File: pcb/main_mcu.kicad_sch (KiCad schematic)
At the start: 16 parts, among them U3 STM32H563VITx

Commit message: tons of work on rf and mcu
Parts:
- added C37, C38: 8pF, symbol Device:C_Small
- added C39, C40: 17pF, symbol Device:C_Small
- added R12, R13: 1k, symbol Device:R_Small
- added Y1: 25mHz 8pf, symbol Device:Crystal_GND24
- added Y2: 32.768kHz 12.5pF, symbol Device:Crystal
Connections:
- net GND: now also C37.2, C38.1, C39.2, C40.1, Y1.2 (G), Y1.4 (G)
- net hse_0: now reaches U3.12 (PH0)
- net hse_0: now also C38.2, Y1.1
- net at U3.13 (PH1): now also R12.2
- net usb1_d-: now reaches U3.70 (PA11)
- net usb1_d+: now reaches U3.71 (PA12)
- net lse_0: now reaches U3.8 (PC14)
- net lse_0: now also C40.2, Y2.1
- net at U3.9 (PC15): now also R13.1
- new net hse_1: C37.1, R12.1, Y1.3
- new net lse_1: C39.1, R13.2, Y2.2
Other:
- note added: "todo: figure out if series resistors are necessary"
- moved on the sheet: C12, C13, U3

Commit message: added missing files, rf stuff done I think (hope)
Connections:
- net gps_tx: now reaches U3.55 (PD8)
- net gps_rx: now reaches U3.56 (PD9)
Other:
- note added: "hse"
- note added: "lse"
- moved on the sheet: C37, C38, Y1

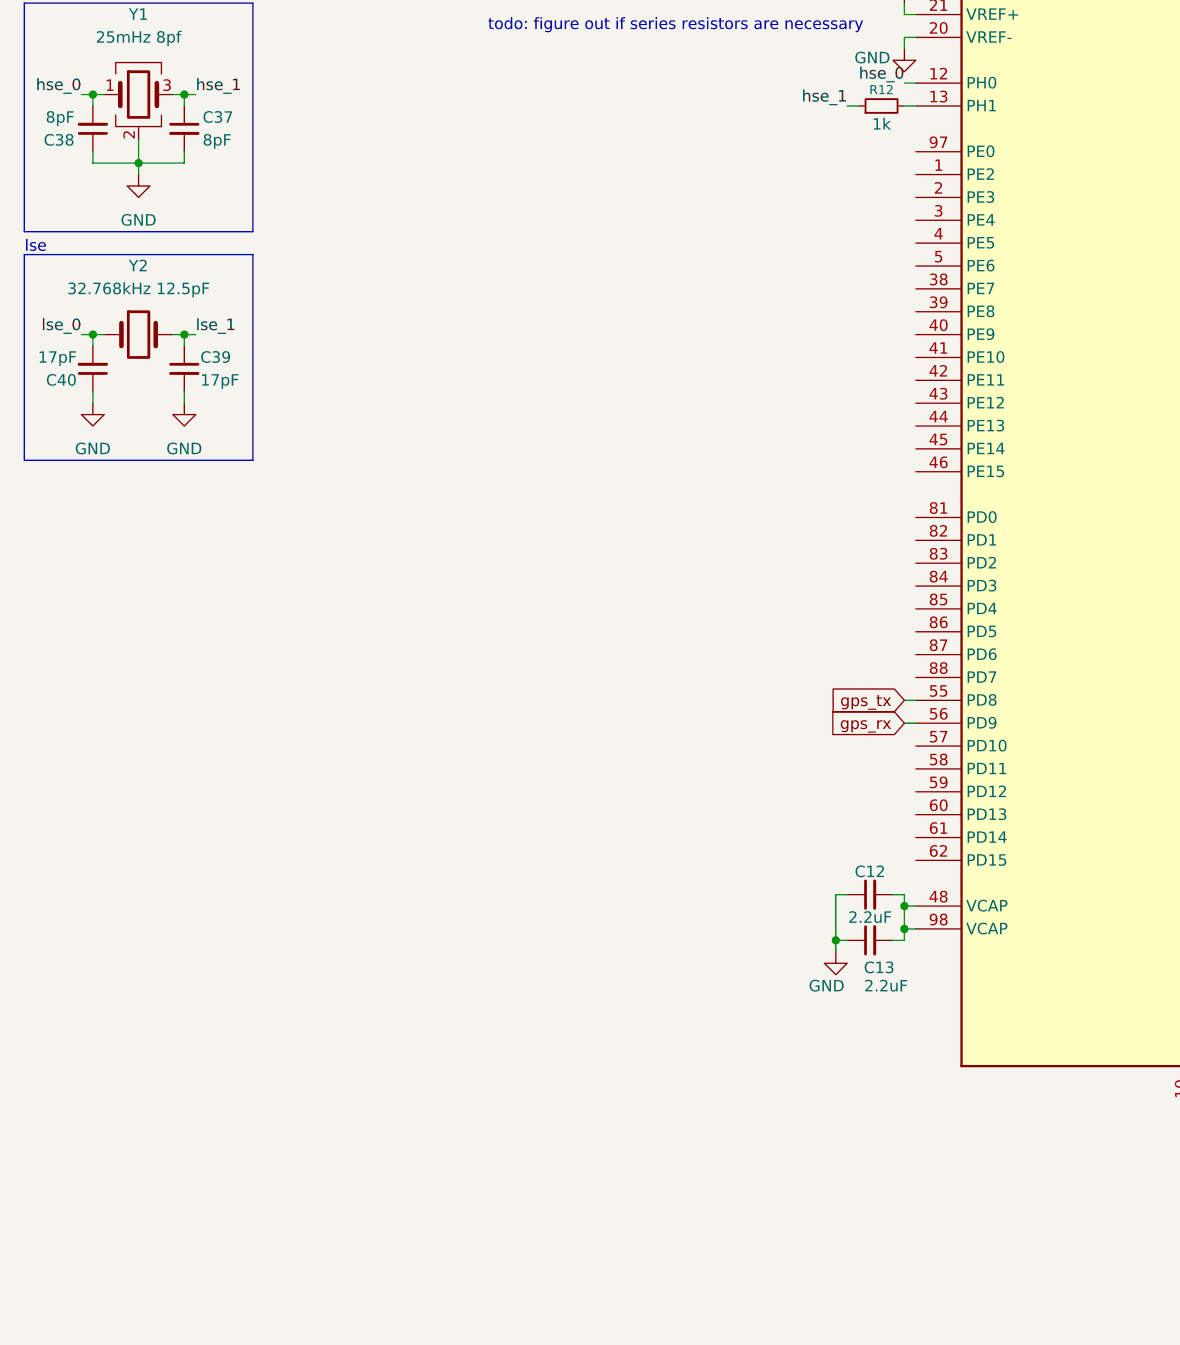
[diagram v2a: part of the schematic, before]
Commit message: sensors pretty much done (still need to add high g_
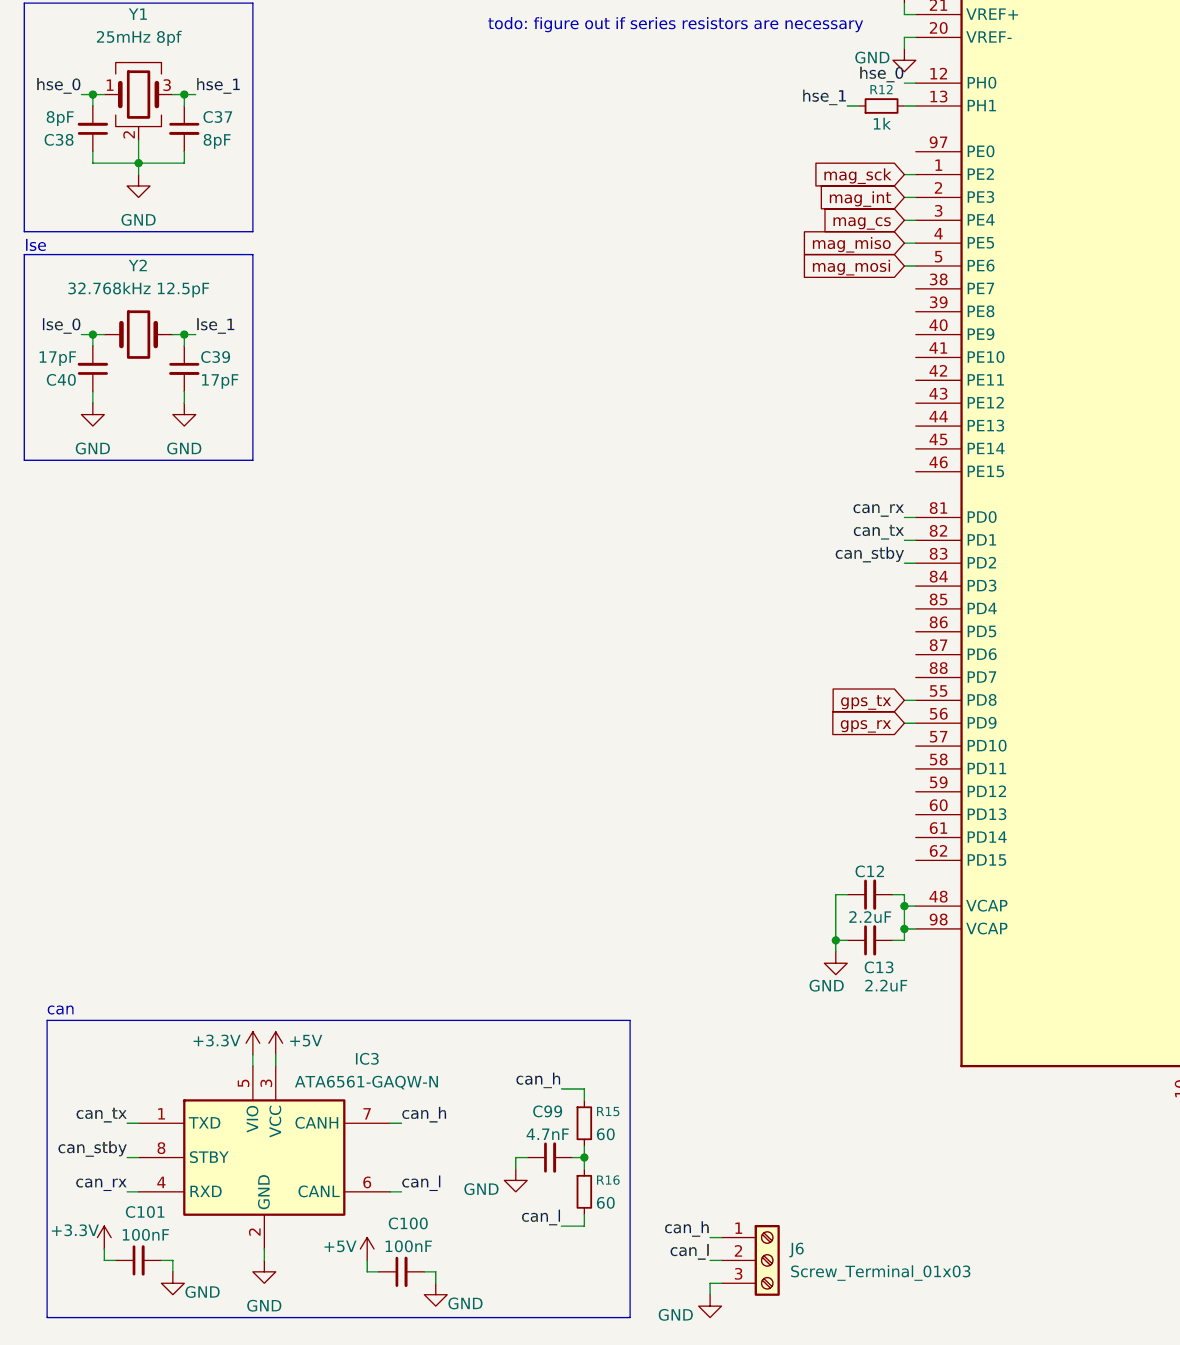
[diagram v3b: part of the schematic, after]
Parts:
- added C100, C101: 100nF, symbol Device:C_Small
- added C99: 4.7nF, symbol Device:C_Small
- added IC3: ATA6561-GAQW-N, SOIC127P600X175-8N, symbol ATA6561-GAQW-N:ATA6561-GAQW-N
- added J6: Screw_Terminal_01x03, symbol Connector:Screw_Terminal_01x03
- added R15, R16: 60, symbol Device:R_Small
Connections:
- net +3.3V: now also C101.1, IC3.5 (VIO)
- net GND: now also C100.2, C101.2, C99.1, IC3.2 (GND), J6.3 (Pin_3)
- net mag_sck: now reaches U3.1 (PE2)
- net mag_int: now reaches U3.2 (PE3)
- net mag_cs: now reaches U3.3 (PE4)
- net mag_miso: now reaches U3.4 (PE5)
- net mag_mosi: now reaches U3.5 (PE6)
- net can_rx: now reaches U3.81 (PD0)
- net can_rx: now also IC3.4 (RXD)
- net can_tx: now reaches U3.82 (PD1)
- net can_tx: now also IC3.1 (TXD)
- net can_stby: now reaches U3.83 (PD2)
- net can_stby: now also IC3.8 (STBY)
- new net: C99.2, R15.2, R16.1
- new net +5V: C100.1, IC3.3 (VCC)
- new net can_h: IC3.7 (CANH), J6.1 (Pin_1), R15.1
- new net can_l: IC3.6 (CANL), J6.2 (Pin_2), R16.2
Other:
- note added: "can"

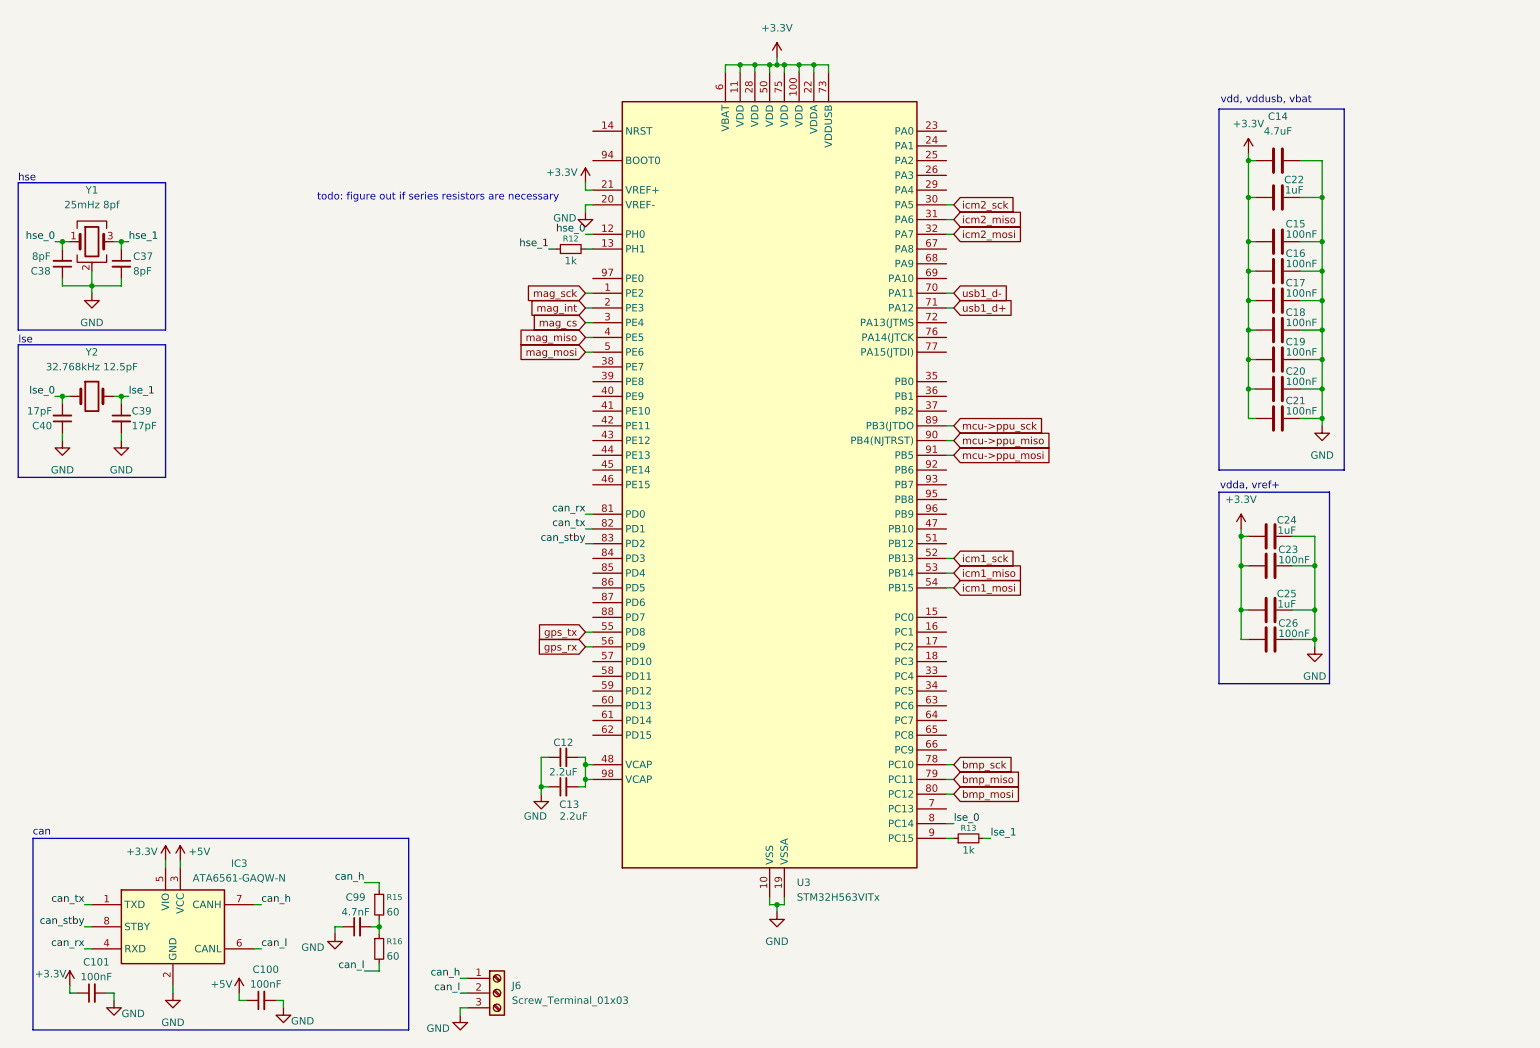
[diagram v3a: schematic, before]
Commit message: got fets figured out (finally), can integrated, a 5v regulator, sensors added - overall great progress!
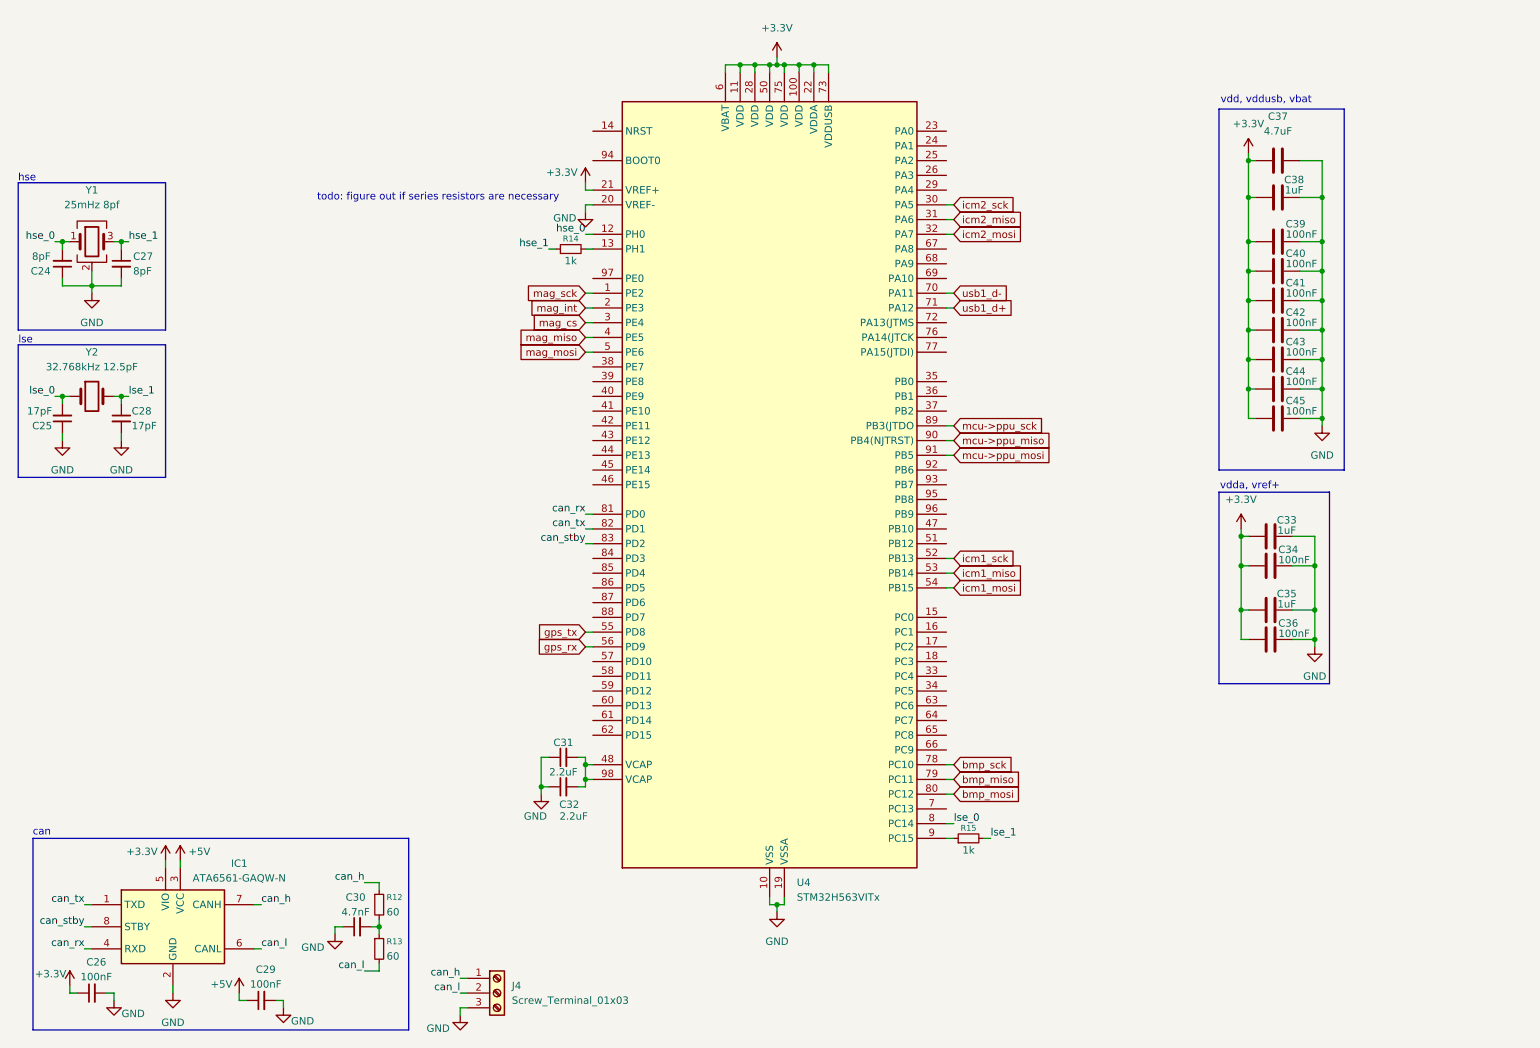
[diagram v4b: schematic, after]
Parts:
- renumbered C38 to C24, C40 to C25, C101 to C26, C37 to C27, C39 to C28, C100 to C29, C99 to C30, C12 to C31, C13 to C32, C24 to C33, C23 to C34, C25 to C35, C26 to C36, C14 to C37, C22 to C38, C15 to C39, C16 to C40, C17 to C41, C18 to C42, C19 to C43, C20 to C44, C21 to C45, IC3 to IC1, J6 to J4, R15 to R12, R16 to R13, R12 to R14, R13 to R15, U3 to U4

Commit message: pretty much everything on schem done, though need to add circuit protection stuff and break out remaining pins
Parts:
- added C18: 100nF, symbol Device:C
- added D5: STATUS, symbol Device:LED
- added J5: Conn_02x04_Top_Bottom, symbol Connector_Generic:Conn_02x04_Top_Bottom
- added JP1: BOOT, TestPoint:TestPoint_2Pads_Pitch2.54mm_Drill0.8mm, symbol Jumper:Jumper_2_Open
- added JP2: RST, TestPoint:TestPoint_2Pads_Pitch2.54mm_Drill0.8mm, symbol Jumper:Jumper_2_Open
- added R14, R15, R16: 10k, symbol Device:R
- added R19: 120, symbol Device:R
- renumbered C24 to C16, C25 to C17, C26 to C19, C27 to C20, C28 to C21, C29 to C22, C30 to C23, C31 to C24, C32 to C25, C33 to C26, C34 to C27, C35 to C28, C36 to C29, C37 to C30, C38 to C31, C39 to C32, C40 to C33, C41 to C34, C42 to C35, C43 to C36, C44 to C37, C45 to C38, R12 to R17, R13 to R18, R14 to R20, R15 to R21
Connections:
- net +3.3V: now also J5.8 (Pin_8), JP1.1 (A), R15.1
- net GND: now also C18.2, J5.4 (Pin_4), JP2.1 (A), R14.2, R19.1
- net rst: now reaches U4.14 (NRST)
- net rst: now also C18.1, J5.3 (Pin_3), JP2.2 (B), R15.2
- net pwm5: now reaches U4.23 (PA0)
- net pwm6: now reaches U4.24 (PA1)
- net pwm7: now reaches U4.25 (PA2)
- net pwm8: now reaches U4.26 (PA3)
- net icm2_cs: now reaches U4.33 (PC4)
- net icm2_int: now reaches U4.34 (PC5)
- net icm1_int: now reaches U4.45 (PE14)
- net icm1_cs: now reaches U4.46 (PE15)
- net mpu_i2c2_scl: now reaches U4.47 (PB10)
- net mpu_i2c2_sda: now reaches U4.51 (PB12)
- net mpu_uart4_rx: now reaches U4.58 (PD11)
- net mpu_uart4_tx: now reaches U4.59 (PD12)
- net icm_fsync: now reaches U4.60 (PD13)
- net pwm1: now reaches U4.63 (PC6)
- net pwm2: now reaches U4.64 (PC7)
- net pwm3: now reaches U4.65 (PC8)
- net pwm4: now reaches U4.66 (PC9)
- net debug_uart_tx: now reaches U4.68 (PA9)
- net debug_uart_tx: now also J5.2 (Pin_2)
- net debug_uart_rx: now reaches U4.69 (PA10)
- net debug_uart_rx: now also J5.1 (Pin_1)
- net swdio: now reaches U4.72 (PA13(JTMS)
- net swdio: now also J5.5 (Pin_5)
- net swclk: now reaches U4.76 (PA14(JTCK)
- net swclk: now also J5.6 (Pin_6)
- net bmp_cs: now reaches U4.84 (PD3)
- net bmp_int: now reaches U4.85 (PD4)
- net mpu_usart2_tx: now reaches U4.86 (PD5)
- net mpu_usart2_rx: now reaches U4.87 (PD6)
- net mpu_i2c1_sda: now reaches U4.93 (PB7)
- net boot: now reaches U4.94 (BOOT0)
- net boot: now also J5.7 (Pin_7), R16.2
- net mpu_i2c1_scl: now reaches U4.95 (PB8)
- net at U4.97 (PE0): now also D5.2 (A)
- net gps_rx renamed gps_mrx
- net gps_tx renamed gps_mtx
- new net: D5.1 (K), R19.2
- new net: JP1.2 (B), R14.1, R16.1
- no-connect marks 0 -> 2
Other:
- note added: "bootsel"
- note added: "debug"
- note added: "reset"
- moved on the sheet: C26, C27, C28, C29, C30, C31, C32, C33, C34, C35, C36, C37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

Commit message: yay schematic pretty much good, though I'm going to have to redo some work to split it into multiple kicad projects so I can have multiple separate boards
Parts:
- C16, C17, C18, C19, C20, C21, C22, C23, C27, C29, C32, C33, C34, C35, C36, C37, C38: footprint (none) -> Capacitor_SMD:C_0402_1005Metric
- C24, C25, C26, C28, C30, C31: footprint (none) -> Capacitor_SMD:C_0603_1608Metric
- IC1: footprint SOIC127P600X175-8N -> ATA6561:SOIC127P600X175-8N
- R14, R15, R16, R17, R18, R20, R21: footprint (none) -> Resistor_SMD:R_0402_1005Metric
- R19: footprint (none) -> Resistor_SMD:R_0603_1608Metric
